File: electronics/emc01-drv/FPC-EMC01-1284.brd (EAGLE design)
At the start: 100 x 86.6 mm, 75 parts, among them J1 USB-MINIB-5PIN, J11 CONN-RECT-16PIN-2ROW, J12 CONN-RECT-16PIN-2ROW, J13 CONN-RECT-16PIN-2ROW, J14 CONN-RECT-16PIN-2ROW, J15 DNP, J16 ICSP, J2 CONN-MOLEX-MICROFIT-6PIN, J3 DNP, J4A MOT-X, J5A MOT-Y, J6A MOT-Z, Q2 2N7002PW, U1 IC-ATMEGA1284P-AU, U2 FT231XS, X1 16Mhz

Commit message: adding new PCB rev
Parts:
- removed STEPSTICK2: STEPSTICK, FirePick:STEPSTICK
- added C111: 0.01 50V, SparkFun-Capacitors:0805
- added C18, C19: 0.1, SparkFun-Capacitors:0805
- added C20: 0.47 6.3V, SparkFun-Capacitors:0805
- added C28: 100 uF, rcl:UD-6,3X7,7_NICHICON
- added R14, R15: 0.2, SparkFun-Resistors:0805
- added R16: 20K, SparkFun-Resistors:0805
- added SJ1, SJ2, SJ3: JUMPER, FirePick:JUMPER-NC
- added U3: IC-DRV8825, FirePick:TSSOP28_PAD
- added VR1: 10K, adafruit:TC33X
- C16: value 100uF -> 0.1 16V; device rcl:PANASONIC_D -> SparkFun-Capacitors:0805
- moved C16 9.52 mm to (23.1, 36.8)
- moved J5A 3.81 mm to (18.4, 27.8)
- moved J5 3.81 mm to (16.4, 26.7)
- moved J8 1.83 mm to (10.5, 37.6)
- moved J8A 1.83 mm to (12.5, 38.8)
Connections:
- removed net N$16: STEPSTICK2.!RESET!, STEPSTICK2.!SLEEP!
- removed net Y1A: J5.2, J5A.2, STEPSTICK2.1A
- removed net Y1B: J5.1, J5A.1, STEPSTICK2.1B
- removed net Y2A: J5.3, J5A.3, STEPSTICK2.2A
- removed net Y2B: J5.4, J5A.4, STEPSTICK2.2B
- new net !ENABLE: U3.21
- new net +12V: C16.1, C18.1, C19.1, C28.+, U3.11, U3.4
- new net CP1: C111.1, U3.1
- new net CP2: C111.2, U3.2
- new net DIR: U3.20
- new net ISENA: R15.2, U3.6
- new net ISENB: R14.2, U3.9
- new net MOD1: SJ2.2, U3.25
- new net MODE0: SJ1.2, U3.24
- new net MODE2: SJ3.2, U3.26
- new net N$1: J5.3, J5A.3, U3.8
- new net N$2: J5.4, J5A.4, U3.10
- new net N$3: R16.1, VR1.3
- new net N$5: J5.2, J5A.2, U3.7
- new net N$6: J5.1, J5A.1, U3.5
- new net STEP: U3.22
- new net V3P3OUT: C20.1, R16.2, SJ1.1, SJ2.1, SJ3.1, U3.15, U3.16, U3.17
- new net VCP: C16.2, U3.3
- new net VREF: U3.12, U3.13, VR1.2
- net !XYZ_ENABLE: no longer STEPSTICK2.!ENABLE!
- net +5V: no longer STEPSTICK2.MS1, STEPSTICK2.MS2, STEPSTICK2.MS3, STEPSTICK2.VDD
- net 12V: no longer C16.+, STEPSTICK2.VMOT
- net GND: now also C18.2, C19.2, C20.2, C28.-, R14.1, R15.1, U3.14, U3.28, U3.PAD, U3.V1, U3.V10, U3.V11, U3.V12, U3.V13, U3.V14, U3.V15, U3.V16, U3.V17, U3.V18, U3.V19, U3.V2, U3.V20, U3.V21, U3.V3, U3.V4, U3.V5, U3.V6, U3.V7, U3.V8, U3.V9, VR1.1; no longer C16.-, STEPSTICK2.GND, STEPSTICK2.GND@2
- net Y_DIR: no longer STEPSTICK2.DIR
- net Y_STEP: no longer STEPSTICK2.STEP
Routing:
- net 12V: track 215.1 -> 157.1 mm
- net +12V: track 0.00 -> 27.4 mm
- net V3P3OUT: track 0.00 -> 21.2 mm
- net Y1B: track 20.1 -> 0.00 mm
- net Y2B: track 20.1 -> 0.00 mm
- net Y2A: track 19.9 -> 0.00 mm
- net Y1A: track 19.9 -> 0.00 mm
- net +5V: track 220.3 -> 202.5 mm, vias 11 -> 10
- net N$2: track 0.00 -> 15.1 mm
- net N$1: track 0.00 -> 14.7 mm
- net N$5: track 0.00 -> 14.6 mm
- net N$6: track 0.00 -> 14.3 mm
- net N$3: track 0.00 -> 8.26 mm
- net MODE0: track 0.00 -> 6.16 mm
- net VREF: track 0.00 -> 5.89 mm
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
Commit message: updated
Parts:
- removed STEPSTICK1, STEPSTICK3: STEPSTICK, FirePick:STEPSTICK
- added C21: 0.1 16V, SparkFun-Capacitors:0805
- added C22, C23: 0.1, SparkFun-Capacitors:0805
- added C24: 0.47 6.3V, SparkFun-Capacitors:0805
- added R17, R18: 0.2, SparkFun-Resistors:0805
- added R19: 20K, SparkFun-Resistors:0805
- added SJ4, SJ5, SJ6: JUMPER, FirePick:JUMPER-NC
- added U5: IC-DRV8825, FirePick:TSSOP28_PAD
- added VR2: 10K, adafruit:TC33X
- C15: value 100uF -> 100 uF; device rcl:PANASONIC_D -> rcl:UD-6,3X7,7_NICHICON
- C17: value 100uF -> 0.01 50V; device rcl:PANASONIC_D -> SparkFun-Capacitors:0805
- moved C17 105.2 mm to (-12.5, -28.2), turned to 0 degrees
- moved C15 38.6 mm to (78.7, 44.4), turned to 60 degrees
- moved J9 16.0 mm to (89.4, 37.4)
- moved J9A 16.0 mm to (87.4, 38.5)
- moved J6A 10.8 mm to (81.5, 27.7)
- moved J6 10.8 mm to (83.4, 26.6)
- moved R15 0.27 mm to (25.3, 32.9)
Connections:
- removed net !ENABLE: U3.21
- removed net +12V: C16.1, C18.1, C19.1, C28.+, U3.11, U3.4
- removed net DIR: U3.20
- removed net N$11: STEPSTICK1.!RESET!, STEPSTICK1.!SLEEP!
- removed net N$24: STEPSTICK3.!RESET!, STEPSTICK3.!SLEEP!
- removed net STEP: U3.22
- removed net Z2A: J6.3, J6A.3, STEPSTICK3.2A
- removed net Z2B: J6.4, J6A.4, STEPSTICK3.2B
- new net CP3: C17.1, U5.1
- new net CP4: C17.2, U5.2
- new net ISENA1: R18.2, U5.6
- new net ISENB1: R17.2, U5.9
- new net MOD2: SJ5.2, U5.25
- new net MODE1: SJ4.2, U5.24
- new net MODE3: SJ6.2, U5.26
- new net N$7: R19.1, VR2.3
- new net N$8: J6.4, J6A.4, U5.7
- new net N$9: J6.3, J6A.3, U5.8
- new net V3P3OUT1: C24.1, R19.2, SJ4.1, SJ5.1, SJ6.1, U5.15, U5.16, U5.17
- new net VCP1: C21.2, U5.3
- new net VREF1: U5.12, U5.13, VR2.2
- net !XYZ_ENABLE: now also U3.21, U5.21; no longer STEPSTICK1.!ENABLE!, STEPSTICK3.!ENABLE!
- net +5V: no longer STEPSTICK1.MS1, STEPSTICK1.MS2, STEPSTICK1.MS3, STEPSTICK1.VDD, STEPSTICK3.MS1, STEPSTICK3.MS2, STEPSTICK3.MS3, STEPSTICK3.VDD
- net 12V: now also C16.1, C18.1, C19.1, C21.1, C22.1, C23.1, C28.+, U3.11, U3.4, U5.11, U5.4; no longer C17.+, STEPSTICK1.VMOT, STEPSTICK3.VMOT
- net GND: now also C22.2, C23.2, C24.2, R17.1, R18.1, U5.14, U5.28, U5.PAD, U5.V1, U5.V10, U5.V11, U5.V12, U5.V13, U5.V14, U5.V15, U5.V16, U5.V17, U5.V18, U5.V19, U5.V2, U5.V20, U5.V21, U5.V3, U5.V4, U5.V5, U5.V6, U5.V7, U5.V8, U5.V9, VR2.1; no longer C17.-, STEPSTICK1.GND, STEPSTICK1.GND@2, STEPSTICK3.GND, STEPSTICK3.GND@2
- net X1A: no longer STEPSTICK1.1A
- net X1B: no longer STEPSTICK1.1B
- net X2A: no longer STEPSTICK1.2A
- net X2B: no longer STEPSTICK1.2B
- net X_DIR: no longer STEPSTICK1.DIR
- net X_STEP: no longer STEPSTICK1.STEP
- net Y_DIR: now also U3.20
- net Y_STEP: now also U3.22
- net Z1A: now also U5.10; no longer STEPSTICK3.1A
- net Z1B: now also U5.5; no longer STEPSTICK3.1B
- net Z_DIR: now also U5.20; no longer STEPSTICK3.DIR
- net Z_STEP: now also U5.22; no longer STEPSTICK3.STEP
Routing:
- net +12V: track 27.4 -> 0.00 mm
- net 12V: track 157.1 -> 181.4 mm
- net Z2B: track 20.0 -> 0.00 mm
- net Z2A: track 19.9 -> 0.00 mm
- net Y_DIR: track 11.1 -> 29.4 mm, vias 1 -> 2
- net Z1B: track 20.0 -> 2.22 mm
- net Z1A: track 19.9 -> 2.27 mm
- net !RESET: track 122.4 -> 106.1 mm
- net GND: track 93.8 -> 77.8 mm, vias 123 -> 110
- net Z_STOP: track 49.7 -> 63.3 mm, vias 2 -> 1
- net Y_STEP: track 14.5 -> 27.2 mm, vias 1 -> 2
- net N$6: track 14.3 -> 19.4 mm
- net N$24: track 4.90 -> 0.00 mm
- net N$11: track 4.49 -> 0.05 mm
- net !XYZ_ENABLE: track 63.6 -> 59.3 mm, vias 3 -> 5
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
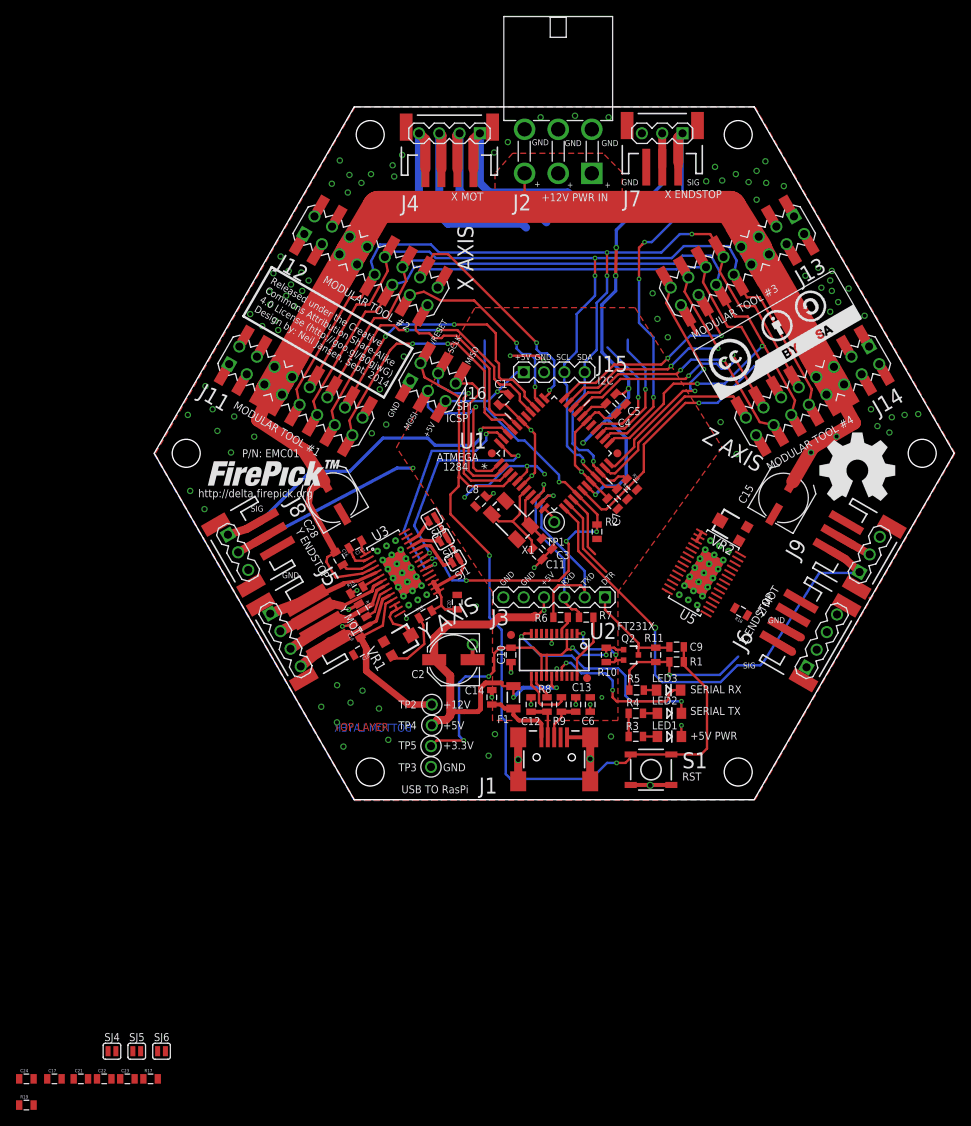
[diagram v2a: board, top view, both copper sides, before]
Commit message: New MCU Conversion
AT90 is hooked up in schematic
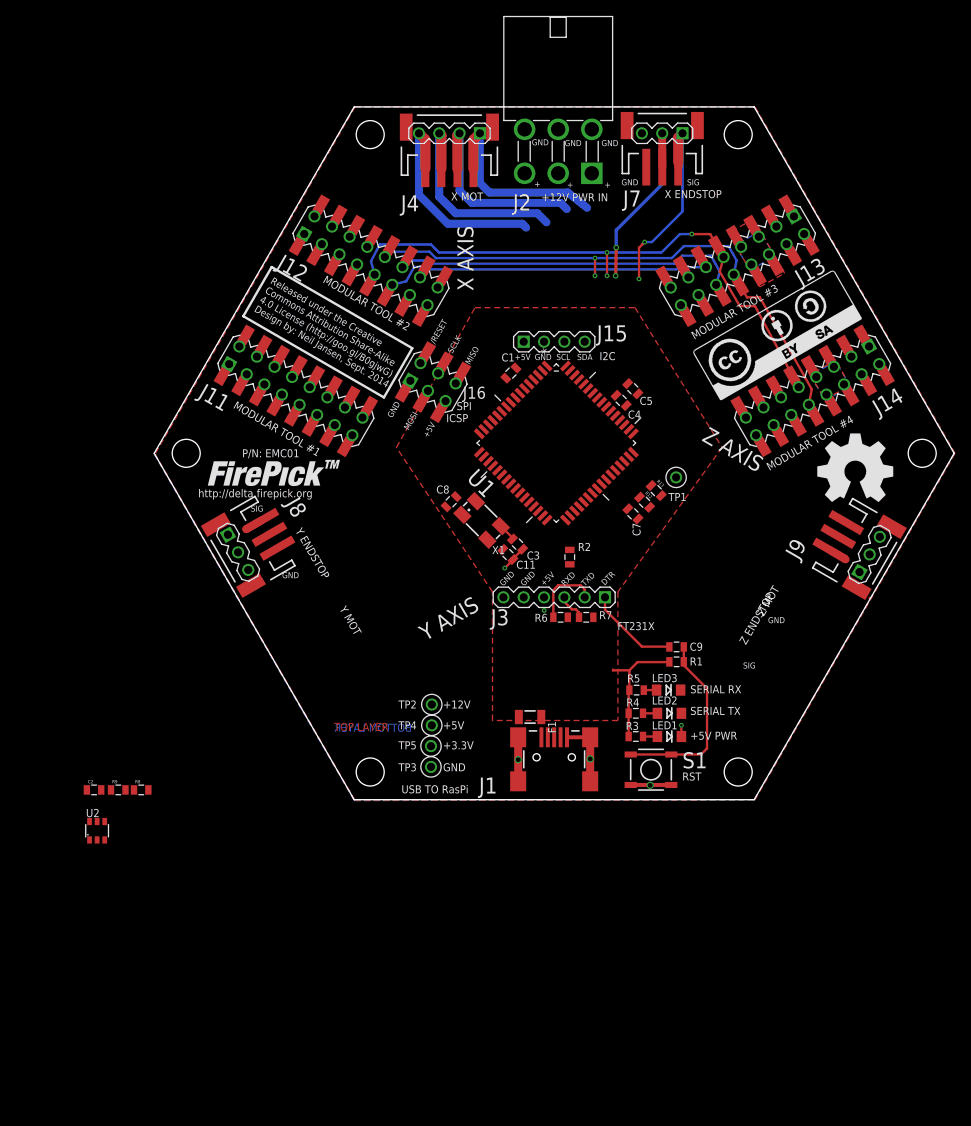
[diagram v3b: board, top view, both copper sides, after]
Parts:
- removed C10, C14, C6: 0.1uF, SparkFun-Capacitors:0805
- removed C111, C17: 0.01 50V, SparkFun-Capacitors:0805
- removed C12, C13: 47pF, SparkFun-Capacitors:0805
- removed C15, C28: 100 uF, rcl:UD-6,3X7,7_NICHICON
- removed C16, C21: 0.1 16V, SparkFun-Capacitors:0805
- removed C18, C19, C22, C23: 0.1, SparkFun-Capacitors:0805
- removed C20, C24: 0.47 6.3V, SparkFun-Capacitors:0805
- removed FID1, FID2, FID3, FID4: FIDUCIAL1X2, SparkFun-Aesthetics:FIDUCIAL-1X2
- removed J5, J6: (no value), !con-lstb:MA04-1
- removed J5A: MOT-Y, FirePick:CONN-JST-PH_2.0MM_4PIN-SMT-RA
- removed J6A: MOT-Z, FirePick:CONN-JST-PH_2.0MM_4PIN-SMT-RA
- removed Q2: 2N7002PW, SparkFun-DiscreteSemi:SOT323
- removed R10, R11: 10k, SparkFun-Resistors:0805
- removed R14, R15, R17, R18: 0.2, SparkFun-Resistors:0805
- removed R16, R19: 20K, SparkFun-Resistors:0805
- removed SJ1, SJ2, SJ3, SJ4, SJ5, SJ6: JUMPER, FirePick:JUMPER-NC
- removed U3, U5: IC-DRV8825, FirePick:TSSOP28_PAD
- removed VR1, VR2: 10K, adafruit:TC33X
- C2: value 4.7uF -> 1uF; device rcl:PANASONIC_D -> SparkFun:0805
- LOGO4: value LOGO-FIREPICK -> LOGO-FIREPICKLARGE
- LOGO6: value LOGO-CC-BY-SA -> LOGO-CC-BY-SALARGE
- R8, R9: value 27 -> 22; device SparkFun-Resistors:0805 -> SparkFun:0805
- U1: value IC-ATMEGA1284P-AU -> AT90USB1287-AU; device FirePick:QFP44 -> Atmel_By_element14_Batch_1-00:QFP80P1600X1600X120-64N
- U2: value FT231XS -> PRTR5V0U4D; device SparkFun-DigitalIC:SSOP20_L -> printrbot:SOT23-6
- X1: value 16Mhz -> 20MHz
- moved U2 61.2 mm to (-7.14, 2.82), turned to 0 degrees
- moved R9 56.4 mm to (-4.50, 7.92), turned to 0 degrees
- moved R8 51.8 mm to (-1.63, 7.92), turned to 0 degrees
- moved C2 47.8 mm to (-7.52, 7.92), turned to 0 degrees
- moved TP1 16.2 mm to (65.2, 47.0)
- moved R2 4.65 mm to (51.9, 37.0)
- moved J15 3.81 mm to (50.0, 64.0)
- moved C11 3.68 mm to (44.2, 37.3)
- moved C3 3.68 mm to (45.4, 38.6)
- moved C8 3.68 mm to (37.1, 43.9)
- moved X1 3.68 mm to (40.9, 41.6)
- moved C1 3.44 mm to (44.6, 60.0)
- moved F1 3.23 mm to (47.0, 17.0), turned to 180 degrees
- moved R13 3.14 mm to (62.7, 45.3)
- moved R12 2.97 mm to (61.3, 43.9)
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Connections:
- removed net CP1: C111.1, U3.1
- removed net CP2: C111.2, U3.2
- removed net CP3: C17.1, U5.1
- removed net CP4: C17.2, U5.2
- removed net DTR_3.3V: Q2.2, R10.1, U2.1
- removed net ISENA: R15.2, U3.6
- removed net ISENA1: R18.2, U5.6
- removed net ISENB: R14.2, U3.9
- removed net ISENB1: R17.2, U5.9
- removed net MOD1: SJ2.2, U3.25
- removed net MOD2: SJ5.2, U5.25
- removed net MODE0: SJ1.2, U3.24
- removed net MODE1: SJ4.2, U5.24
- removed net MODE2: SJ3.2, U3.26
- removed net MODE3: SJ6.2, U5.26
- removed net N$23: R8.2, U2.12
- removed net N$25: R9.2, U2.11
- removed net N$3: R16.1, VR1.3
- removed net N$5: J5.2, J5A.2, U3.7
- removed net N$6: J5.1, J5A.1, U3.5
- removed net N$7: R19.1, VR2.3
- removed net N$8: J6.4, J6A.4, U5.7
- removed net N$9: J6.3, J6A.3, U5.8
- removed net V3P3OUT: C20.1, R16.2, SJ1.1, SJ2.1, SJ3.1, U3.15, U3.16, U3.17
- removed net V3P3OUT1: C24.1, R19.2, SJ4.1, SJ5.1, SJ6.1, U5.15, U5.16, U5.17
- removed net VCP: C16.2, U3.3
- removed net VCP1: C21.2, U5.3
- removed net VREF: U3.12, U3.13, VR1.2
- removed net VREF1: U5.12, U5.13, VR2.2
- removed net Z1A: J6.2, J6A.2, U5.10
- removed net Z1B: J6.1, J6A.1, U5.5
- new net SDCS: U1.10
- new net UCAP: C2.2, U1.7
- new net VBUS: U1.8, U2.5
- net !RESET: now also U1.20; no longer U1.4
- net !XYZ_ENABLE: now also U1.35; no longer U1.15, U3.21, U5.21
- net +5V: now also U1.21, U1.3, U1.52, U1.64; no longer C2.+, C6.1, R11.2, U1.17, U1.27, U1.38, U1.5, U2.15
- net 12V: no longer C15.+, C16.1, C18.1, C19.1, C21.1, C22.1, C23.1, C28.+, U3.11, U3.4, U5.11, U5.4
- net 3.3V: no longer C10.1, Q2.1, R10.2, U2.13, U2.14, U2.3
- net AREF: now also U1.62; no longer U1.29
- net AVR_RXD: now also U1.27; no longer U1.9
- net AVR_TXD: now also U1.28; no longer U1.10
- net D+: now also R9.2, U1.5, U2.1; no longer C13.1, J1.D+, R9.1
- net D-: now also R8.2, U1.4, U2.3; no longer C12.1, J1.D-, R8.1
- net DTR: no longer Q2.3, R11.1
- net GND: now also C2.1, U1.22, U1.53, U1.63, U2.2; no longer C10.2, C12.2, C13.2, C14.2, C15.-, C18.2, C19.2, C2.-, C20.2, C22.2, C23.2, C24.2, C28.-, C6.2, R14.1, R15.1, R17.1, R18.1, U1.18, U1.28, U1.39, U2.16, U2.6, U3.14, U3.28, U3.PAD, U3.V1, U3.V10, U3.V11, U3.V12, U3.V13, U3.V14, U3.V15, U3.V16, U3.V17, U3.V18, U3.V19, U3.V2, U3.V20, U3.V21, U3.V3, U3.V4, U3.V5, U3.V6, U3.V7, U3.V8, U3.V9, U5.14, U5.28, U5.PAD, U5.V1, U5.V10, U5.V11, U5.V12, U5.V13, U5.V14, U5.V15, U5.V16, U5.V17, U5.V18, U5.V19, U5.V2, U5.V20, U5.V21, U5.V3, U5.V4, U5.V5, U5.V6, U5.V7, U5.V8, U5.V9, VR1.1, VR2.1
- net MISO: now also U1.13; no longer U1.2
- net MOSI: now also U1.12; no longer U1.1
- net N$1: now also J1.D-, R8.1; no longer J5.3, J5A.3, U3.8
- net N$2: now also J1.D+, R9.1; no longer J5.4, J5A.4, U3.10
- net RXD: no longer U2.4
- net RXLED: no longer U2.17
- net SCL: now also U1.25; no longer U1.19
- net SCLK: now also U1.11; no longer U1.3
- net SDA: now also U1.26; no longer U1.20
- net SPARE: now also U1.43; no longer U1.11
- net TOOL1_AIN: now also U1.61; no longer U1.37
- net TOOL1_DOUT: now also U1.60; no longer U1.36
- net TOOL1_ENABLE: now also U1.17; no longer U1.41
- net TOOL2_AIN: now also U1.59; no longer U1.35
- net TOOL2_DOUT: now also U1.58; no longer U1.34
- net TOOL2_ENABLE: now also U1.16; no longer U1.40
- net TOOL3_AIN: now also U1.56; no longer U1.32
- net TOOL3_DOUT: now also U1.57; no longer U1.33
- net TOOL3_ENABLE: now also U1.15; no longer U1.22
- net TOOL4_AIN: now also U1.54; no longer U1.30
- net TOOL4_DOUT: now also U1.55; no longer U1.31
- net TOOL4_ENABLE: now also U1.14; no longer U1.21
- net TOOL_DIR: now also U1.44; no longer U1.16
- net TOOL_STEP: now also U1.45; no longer U1.23
- net TXD: no longer U2.20
- net TXLED: no longer U2.10
- net VUSB: no longer C14.1
- net XTAL1: now also U1.24; no longer U1.8
- net XTAL2: now also U1.23; no longer U1.7
- net X_DIR: now also U1.50; no longer U1.25
- net X_STEP: now also U1.51; no longer U1.26
- net X_STOP: now also U1.9; no longer U1.24
- net Y_DIR: now also U1.48; no longer U1.43, U3.20
- net Y_STEP: now also U1.49; no longer U1.44, U3.22
- net Y_STOP: now also U1.18; no longer U1.42
- net Z_DIR: now also U1.46; no longer U1.13, U5.20
- net Z_STEP: now also U1.47; no longer U1.14, U5.22
- net Z_STOP: now also U1.19; no longer U1.12
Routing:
- net 12V: track 181.4 -> 0.00 mm
- net +5V: track 200.2 -> 40.4 mm, vias 15 -> 3
- net !RESET: track 106.1 -> 23.7 mm, vias 2 -> 0
- net TOOL_DIR: track 113.7 -> 40.6 mm, vias 2 -> 0
- net TOOL_STEP: track 108.9 -> 43.5 mm, vias 2 -> 0
- net Z_STOP: track 63.3 -> 2.39 mm, vias 1 -> 0
- net !XYZ_ENABLE: track 59.3 -> 0.00 mm, vias 5 -> 0
- net GND: track 77.8 -> 23.7 mm, vias 110 -> 5
- net SDA: track 125.7 -> 73.3 mm, vias 4 -> 3
- net SCL: track 122.3 -> 70.3 mm, vias 3 -> 2
- net 3.3V: track 45.0 -> 0.00 mm, vias 4 -> 0
- net Y_STOP: track 46.6 -> 2.33 mm, vias 2 -> 1
- net TOOL1_AIN: track 38.7 -> 0.00 mm, vias 2 -> 0
- net TOOL1_DOUT: track 37.2 -> 0.00 mm, vias 2 -> 0
- net TOOL1_ENABLE: track 35.2 -> 0.00 mm, vias 2 -> 0
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- removed copper zone on layer 1, net GND
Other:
- board text removed: "1284"
- board text removed: "ATMEGA"
